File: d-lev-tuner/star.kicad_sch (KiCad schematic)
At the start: 13 parts

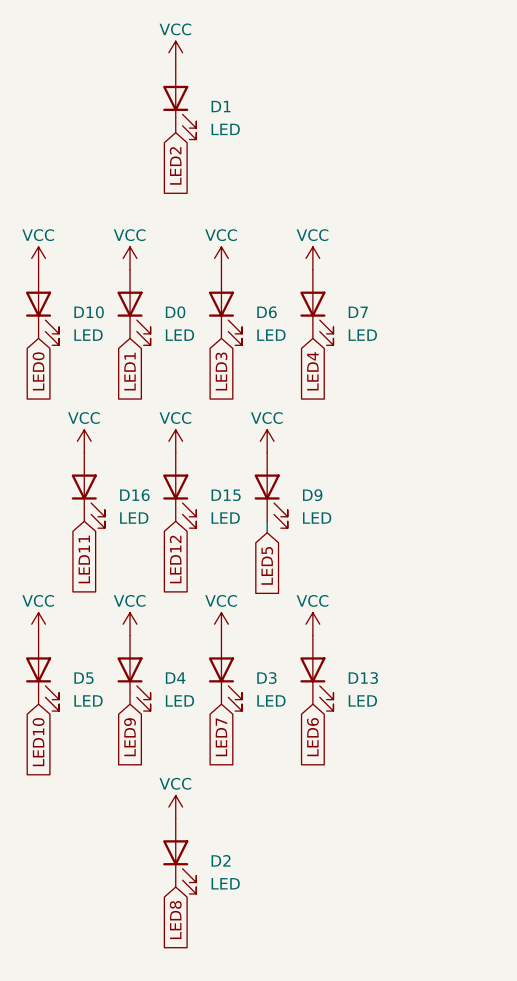
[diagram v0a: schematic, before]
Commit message: tuner: fix led footprints, reroute, place vias artistically
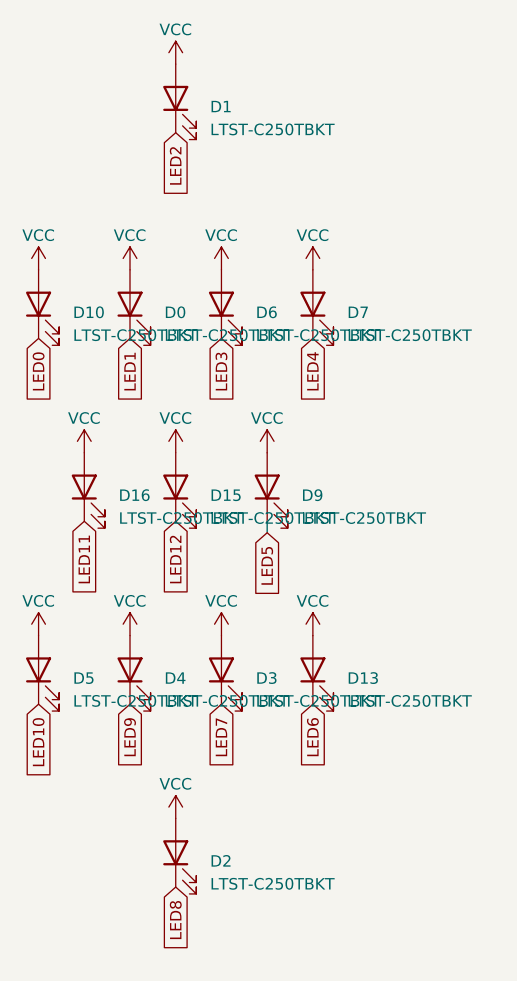
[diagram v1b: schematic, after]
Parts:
- D0, D1, D10, D13, D15, D16, D2, D3, D4, D5, D6, D7, D9: value LED -> LTST-C250TBKT
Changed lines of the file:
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@@
       (effects (font (size 1.27 1.27)) (justify right))
     )
-    (property "Value" "LED" (at 144.78 103.8225 90)
+    (property "Value" "LTST-C250TBKT" (at 144.78 103.8225 90)
       (effects (font (size 1.27 1.27)) (justify right))
     )
@@
       (effects (font (size 1.27 1.27)) hide)
     )
-    (property "Datasheet" "~" (at 140.97 100.33 0)
+    (property "Datasheet" "https://www.mouser.com/datasheet/2/239/lite-on_lites11853-1-1737274.pdf" (at 140.97 100.33 0)
       (effects (font (size 1.27 1.27)) hide)
     )
@@
       (effects (font (size 1.27 1.27)) (justify right))
     )
-    (property "Value" "LED" (at 139.7 124.1425 90)
+    (property "Value" "LTST-C250TBKT" (at 139.7 124.1425 90)
       (effects (font (size 1.27 1.27)) (justify right))
     )
@@
       (effects (font (size 1.27 1.27)) hide)
     )
-    (property "Datasheet" "~" (at 135.89 120.65 0)
+    (property "Datasheet" "https://www.mouser.com/datasheet/2/239/lite-on_lites11853-1-1737274.pdf" (at 135.89 120.65 0)
       (effects (font (size 1.27 1.27)) hide)
     )
@@
       (effects (font (size 1.27 1.27)) (justify right))
     )
-    (property "Value" "LED" (at 144.78 144.4625 90)
+    (property "Value" "LTST-C250TBKT" (at 144.78 144.4625 90)
       (effects (font (size 1.27 1.27)) (justify right))
     )
@@
       (effects (font (size 1.27 1.27)) hide)
     )
-    (property "Datasheet" "~" (at 140.97 140.97 0)
+    (property "Datasheet" "https://www.mouser.com/datasheet/2/239/lite-on_lites11853-1-1737274.pdf" (at 140.97 140.97 0)
       (effects (font (size 1.27 1.27)) hide)
     )
@@
       (effects (font (size 1.27 1.27)) (justify right))
     )
-    (property "Value" "LED" (at 144.78 60.6425 90)
+    (property "Value" "LTST-C250TBKT" (at 144.78 60.6425 90)
       (effects (font (size 1.27 1.27)) (justify right))
     )
@@
       (effects (font (size 1.27 1.27)) hide)
     )
-    (property "Datasheet" "~" (at 140.97 57.15 0)
+    (property "Datasheet" "https://www.mouser.com/datasheet/2/239/lite-on_lites11853-1-1737274.pdf" (at 140.97 57.15 0)
       (effects (font (size 1.27 1.27)) hide)
     )
@@
       (effects (font (size 1.27 1.27)) (justify right))
     )
-    (property "Value" "LED" (at 160.02 124.1425 90)
+    (property "Value" "LTST-C250TBKT" (at 160.02 124.1425 90)
       (effects (font (size 1.27 1.27)) (justify right))
     )
@@
       (effects (font (size 1.27 1.27)) hide)
     )
-    (property "Datasheet" "~" (at 156.21 120.65 0)
+    (property "Datasheet" "https://www.mouser.com/datasheet/2/239/lite-on_lites11853-1-1737274.pdf" (at 156.21 120.65 0)
       (effects (font (size 1.27 1.27)) hide)
     )
@@
       (effects (font (size 1.27 1.27)) (justify right))
     )
-    (property "Value" "LED" (at 160.02 83.5025 90)
+    (property "Value" "LTST-C250TBKT" (at 160.02 83.5025 90)
       (effects (font (size 1.27 1.27)) (justify right))
     )
@@
       (effects (font (size 1.27 1.27)) hide)
     )
-    (property "Datasheet" "~" (at 156.21 80.01 0)
+    (property "Datasheet" "https://www.mouser.com/datasheet/2/239/lite-on_lites11853-1-1737274.pdf" (at 156.21 80.01 0)
       (effects (font (size 1.27 1.27)) hide)
     )
@@
       (effects (font (size 1.27 1.27)) (justify right))
     )
-    (property "Value" "LED" (at 149.86 124.1425 90)
+    (property "Value" "LTST-C250TBKT" (at 149.86 124.1425 90)
       (effects (font (size 1.27 1.27)) (justify right))
     )
@@
       (effects (font (size 1.27 1.27)) hide)
     )
-    (property "Datasheet" "~" (at 146.05 120.65 0)
+    (property "Datasheet" "https://www.mouser.com/datasheet/2/239/lite-on_lites11853-1-1737274.pdf" (at 146.05 120.65 0)
       (effects (font (size 1.27 1.27)) hide)
     )
@@
       (effects (font (size 1.27 1.27)) (justify right))
     )
-    (property "Value" "LED" (at 129.54 124.1425 90)
+    (property "Value" "LTST-C250TBKT" (at 129.54 124.1425 90)
       (effects (font (size 1.27 1.27)) (justify right))
     )
@@
       (effects (font (size 1.27 1.27)) hide)
     )
-    (property "Datasheet" "~" (at 125.73 120.65 0)
+    (property "Datasheet" "https://www.mouser.com/datasheet/2/239/lite-on_lites11853-1-1737274.pdf" (at 125.73 120.65 0)
       (effects (font (size 1.27 1.27)) hide)
     )
@@
       (effects (font (size 1.27 1.27)) (justify right))
     )
-    (property "Value" "LED" (at 139.7 83.5025 90)
+    (property "Value" "LTST-C250TBKT" (at 139.7 83.5025 90)
       (effects (font (size 1.27 1.27)) (justify right))
     )
@@
       (effects (font (size 1.27 1.27)) hide)
     )
-    (property "Datasheet" "~" (at 135.89 80.01 0)
+    (property "Datasheet" "https://www.mouser.com/datasheet/2/239/lite-on_lites11853-1-1737274.pdf" (at 135.89 80.01 0)
       (effects (font (size 1.27 1.27)) hide)
     )
@@
       (effects (font (size 1.27 1.27)) (justify right))
     )
-    (property "Value" "LED" (at 154.94 103.8225 90)
+    (property "Value" "LTST-C250TBKT" (at 154.94 103.8225 90)
       (effects (font (size 1.27 1.27)) (justify right))
     )
@@
       (effects (font (size 1.27 1.27)) hide)
     )
-    (property "Datasheet" "~" (at 151.13 100.33 0)
+    (property "Datasheet" "https://www.mouser.com/datasheet/2/239/lite-on_lites11853-1-1737274.pdf" (at 151.13 100.33 0)
       (effects (font (size 1.27 1.27)) hide)
     )
@@
       (effects (font (size 1.27 1.27)) (justify right))
     )
-    (property "Value" "LED" (at 129.54 83.5025 90)
+    (property "Value" "LTST-C250TBKT" (at 129.54 83.5025 90)
       (effects (font (size 1.27 1.27)) (justify right))
     )
@@
       (effects (font (size 1.27 1.27)) hide)
     )
-    (property "Datasheet" "~" (at 125.73 80.01 0)
+    (property "Datasheet" "https://www.mouser.com/datasheet/2/239/lite-on_lites11853-1-1737274.pdf" (at 125.73 80.01 0)
       (effects (font (size 1.27 1.27)) hide)
     )
@@
       (effects (font (size 1.27 1.27)) (justify right))
     )
-    (property "Value" "LED" (at 134.62 103.8225 90)
+    (property "Value" "LTST-C250TBKT" (at 134.62 103.8225 90)
       (effects (font (size 1.27 1.27)) (justify right))
     )
@@
       (effects (font (size 1.27 1.27)) hide)
     )
-    (property "Datasheet" "~" (at 130.81 100.33 0)
+    (property "Datasheet" "https://www.mouser.com/datasheet/2/239/lite-on_lites11853-1-1737274.pdf" (at 130.81 100.33 0)
       (effects (font (size 1.27 1.27)) hide)
     )
@@
       (effects (font (size 1.27 1.27)) (justify right))
     )
-    (property "Value" "LED" (at 149.86 83.5025 90)
+    (property "Value" "LTST-C250TBKT" (at 149.86 83.5025 90)
       (effects (font (size 1.27 1.27)) (justify right))
     )
@@
       (effects (font (size 1.27 1.27)) hide)
     )
-    (property "Datasheet" "~" (at 146.05 80.01 0)
-      (effects (font (size 1.27 1.27)) hide)
-    )
+    (property "Datasheet" "https://www.mouser.com/datasheet/2/239/lite-on_lites11853-1-1737274.pdf" (at 146.05 80.01 0)
+      (effects (font (size 1.27 1.27)) hide)
+    )

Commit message: Add iBOMs and additional part numbers
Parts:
- D0, D1, D10, D13, D15, D16, D2, D3, D4, D5, D6, D7, D9: MPN (none) -> LTST-C250TBKT; Supplier (none) -> Mouser; Supplier URL (none) -> https://www.mouser.com/ProductDetail/859-LTST-C250TBKT
